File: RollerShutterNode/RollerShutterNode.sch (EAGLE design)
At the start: 32 parts, among them IC2 AT25DF512C-SSHN-B, U1 MMBT2222A-7-F, U2 MMBT2222A-7-F, U3 LM321

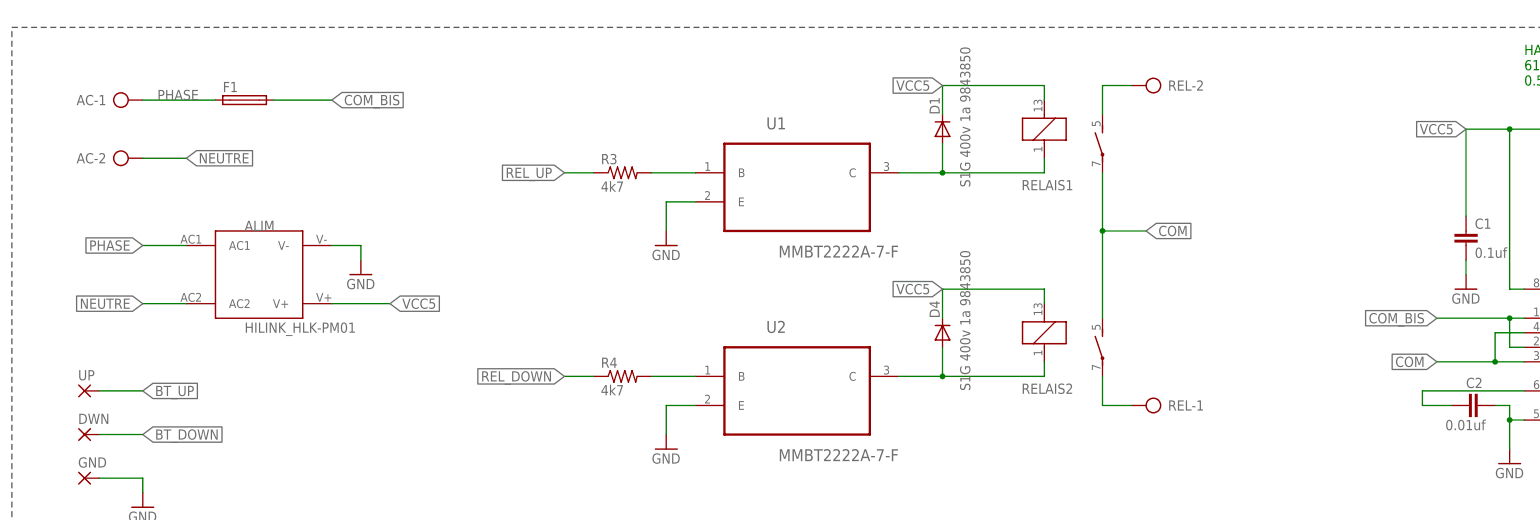
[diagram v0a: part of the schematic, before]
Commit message: fuse removed, added 12-220v motor control
Need to use external fuse and snubber if needed
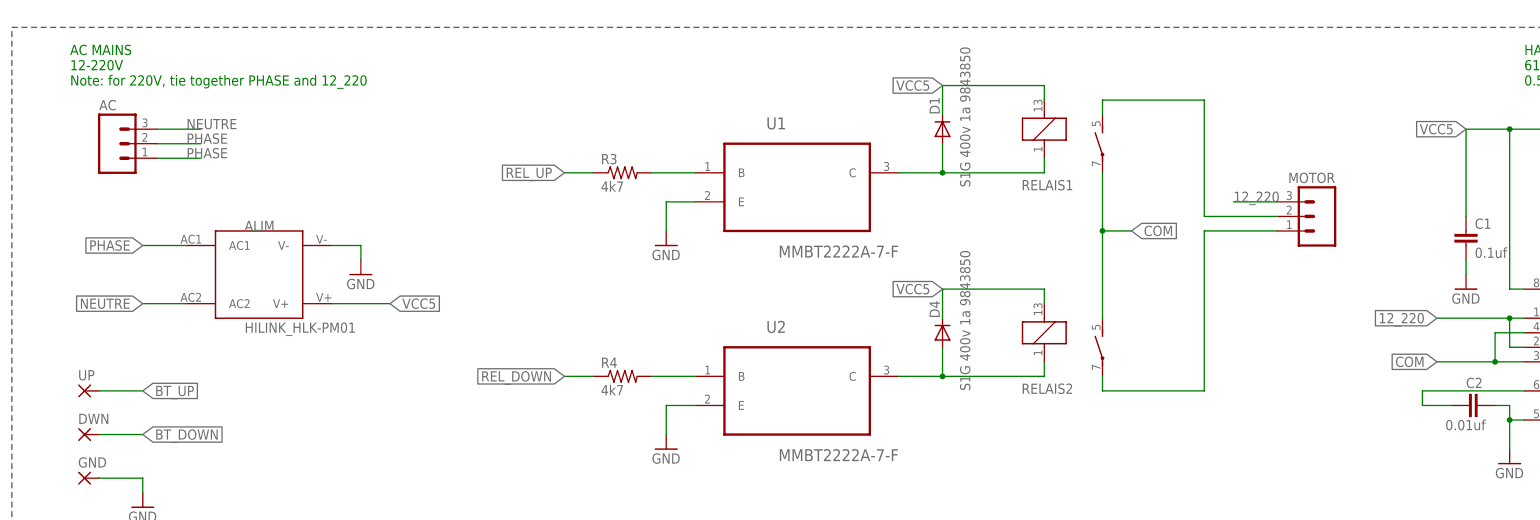
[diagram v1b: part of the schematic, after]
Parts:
- removed F1: (no value), fuse:TE5
- removed REL: (no value), ProgrammateurFilPilote_1.2:AK500/2
- added MOTOR: (no value), SparkFun-Connectors:M03SCREW
- AC: device ProgrammateurFilPilote_1.2:AK500/2 -> SparkFun-Connectors:M03SCREW
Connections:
- removed net COM_BIS: ACS1.IP+, ACS1.IP+_2, F1.2
- new net 12_220: ACS1.IP+, ACS1.IP+_2, MOTOR.3
- net N$7: now also MOTOR.2; no longer REL-2.KL
- net N$9: now also MOTOR.1; no longer REL-1.KL
- net NEUTRE: now also AC.3; no longer AC-2.KL
- net PHASE: now also AC.1, AC.2; no longer AC-1.KL, F1.1
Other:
- note added: "AC MAINS 12-220V Note: for 220V, tie together PHASE and 12_220"
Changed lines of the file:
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@@
 <attribute name="OC_NEWARK" value=""/>
 </part>
-<part name="F1" library="fuse" deviceset="TE5" device=""/>
 <part name="R4" library="SparkFun-Resistors" deviceset="RESISTOR" device="1206" value="4k7"/>
 <part name="GND15" library="supply1" deviceset="GND" device=""/>
@@
 <part name="U1" library="pmo_lib" deviceset="MMBT2222A-7-F" device=""/>
 <part name="U2" library="pmo_lib" deviceset="MMBT2222A-7-F" device=""/>
-<part name="AC" library="ProgrammateurFilPilote_1.2" deviceset="AK500/2" device=""/>
-<part name="REL" library="ProgrammateurFilPilote_1.2" deviceset="AK500/2" device=""/>
 <part name="ALIM" library="pmo_lib" deviceset="HILINK_HLK-PM01" device=""/>
 <part name="GND1" library="SparkFun-Aesthetics" deviceset="GND" device=""/>
@@
 <part name="GND4" library="SparkFun-Aesthetics" deviceset="GND" device=""/>
 <part name="ANT_RFM" library="wirepad" deviceset="SMD2" device=""/>
+<part name="AC" library="SparkFun-Connectors" deviceset="M03" device="SCREW"/>
+<part name="MOTOR" library="SparkFun-Connectors" deviceset="M03" device="SCREW"/>
 </parts>
 <sheets>
@@
 610mV/A
 0.5A -&gt; 93 of 1023 ADC 10bits</text>
+<text x="-33.02" y="106.68" size="1.778" layer="91">AC MAINS
+12-220V
+Note: for 220V, tie together PHASE and 12_220</text>
 </plain>
 <instances>
@@
 </instance>
 <instance part="RELAIS1" gate="2" x="147.32" y="96.52" smashed="yes"/>
-<instance part="F1" gate="1" x="-2.54" y="104.14"/>
 <instance part="R4" gate="G$1" x="63.5" y="55.88"/>
 <instance part="GND15" gate="1" x="71.12" y="43.18"/>
@@
 <instance part="U1" gate="A" x="93.98" y="91.44"/>
 <instance part="U2" gate="A" x="93.98" y="55.88"/>
-<instance part="AC" gate="-1" x="-25.4" y="104.14"/>
-<instance part="AC" gate="-2" x="-25.4" y="93.98"/>
-<instance part="REL" gate="-1" x="157.48" y="50.8" rot="R180"/>
-<instance part="REL" gate="-2" x="157.48" y="106.68" rot="R180"/>
 <instance part="ALIM" gate="G$1" x="0" y="73.66"/>
 <instance part="GND1" gate="1" x="17.78" y="73.66"/>
@@
 <instance part="GND4" gate="1" x="60.96" y="-33.02"/>
 <instance part="ANT_RFM" gate="1" x="233.68" y="-15.24" rot="R270"/>
+<instance part="AC" gate="G$1" x="-25.4" y="96.52"/>
+<instance part="MOTOR" gate="G$1" x="185.42" y="83.82" rot="MR0"/>
 </instances>
 <busses>
@@
 </segment>
 </net>
-<net name="COM_BIS" class="0">
-<segment>
-<pinref part="ACS1" gate="A" pin="IP+_2"/>
-<wire x1="220.98" y1="66.04" x2="218.44" y2="66.04" width="0.1524" layer="91"/>
-<wire x1="218.44" y1="66.04" x2="218.44" y2="60.96" width="0.1524" layer="91"/>
-<pinref part="ACS1" gate="A" pin="IP+"/>
-<wire x1="218.44" y1="60.96" x2="220.98" y2="60.96" width="0.1524" layer="91"/>
-<junction x="218.44" y="66.04"/>
-<wire x1="218.44" y1="66.04" x2="205.74" y2="66.04" width="0.1524" layer="91"/>
-<label x="205.74" y="66.04" size="1.778" layer="95" rot="R180" xref="yes"/>
-</segment>
-<segment>
-<wire x1="2.54" y1="104.14" x2="12.7" y2="104.14" width="0.1524" layer="91"/>
-<label x="12.7" y="104.14" size="1.778" layer="95" xref="yes"/>
-<pinref part="F1" gate="1" pin="2"/>
-</segment>
-</net>
 <net name="N$4" class="0">
 <segment>
@@
 <junction x="147.32" y="81.28"/>
 <wire x1="147.32" y1="81.28" x2="147.32" y2="66.04" width="0.1524" layer="91"/>
-<wire x1="147.32" y1="81.28" x2="154.94" y2="81.28" width="0.1524" layer="91"/>
-<label x="154.94" y="81.28" size="1.778" layer="95" xref="yes"/>
+<wire x1="147.32" y1="81.28" x2="152.4" y2="81.28" width="0.1524" layer="91"/>
+<label x="152.4" y="81.28" size="1.778" layer="95" xref="yes"/>
 </segment>
 <segment>
@@
 <net name="PHASE" class="0">
 <segment>
-<pinref part="AC" gate="-1" pin="KL"/>
-<pinref part="F1" gate="1" pin="1"/>
-<wire x1="-20.32" y1="104.14" x2="-7.62" y2="104.14" width="0.1524" layer="91"/>
-<label x="-17.78" y="104.14" size="1.778" layer="95"/>
-</segment>
-<segment>
 <pinref part="ALIM" gate="G$1" pin="AC1"/>
 <wire x1="-12.7" y1="78.74" x2="-20.32" y2="78.74" width="0.1524" layer="91"/>
 <label x="-20.32" y="78.74" size="1.778" layer="95" rot="R180" xref="yes"/>
 </segment>
+<segment>
+<pinref part="AC" gate="G$1" pin="2"/>
+<wire x1="-17.78" y1="96.52" x2="-10.16" y2="96.52" width="0.1524" layer="91"/>
+<label x="-12.7" y="96.52" size="1.778" layer="95"/>
+</segment>
+<segment>
+<pinref part="AC" gate="G$1" pin="1"/>
+<wire x1="-17.78" y1="93.98" x2="-10.16" y2="93.98" width="0.1524" layer="91"/>
+<label x="-12.7" y="93.98" size="1.778" layer="95"/>
+</segment>
 </net>
 <net name="NEUTRE" class="0">
-<segment>
-<pinref part="AC" gate="-2" pin="KL"/>
-<wire x1="-20.32" y1="93.98" x2="-12.7" y2="93.98" width="0.1524" layer="91"/>
-<label x="-12.7" y="93.98" size="1.778" layer="95" xref="yes"/>
-</segment>
 <segment>
 <pinref part="ALIM" gate="G$1" pin="AC2"/>
@@
 <label x="-20.32" y="68.58" size="1.778" layer="95" rot="R180" xref="yes"/>
 </segment>
-</net>
-<net name="N$7" class="0">
-<segment>
-<pinref part="RELAIS1" gate="2" pin="S"/>
-<wire x1="147.32" y1="101.6" x2="147.32" y2="106.68" width="0.1524" layer="91"/>
-<pinref part="REL" gate="-2" pin="KL"/>
-<wire x1="152.4" y1="106.68" x2="147.32" y2="106.68" width="0.1524" layer="91"/>
-</segment>
-</net>
-<net name="N$9" class="0">
-<segment>
-<pinref part="RELAIS2" gate="2" pin="P"/>
-<wire x1="147.32" y1="55.88" x2="147.32" y2="50.8" width="0.1524" layer="91"/>
-<pinref part="REL" gate="-1" pin="KL"/>
-<wire x1="152.4" y1="50.8" x2="147.32" y2="50.8" width="0.1524" layer="91"/>
+<segment>
+<pinref part="AC" gate="G$1" pin="3"/>
+<wire x1="-17.78" y1="99.06" x2="-10.16" y2="99.06" width="0.1524" layer="91"/>
+<label x="-12.7" y="99.06" size="1.778" layer="95"/>
 </segment>
 </net>
@@
 </segment>
 </net>
+<net name="12_220" class="0">
+<segment>
+<pinref part="ACS1" gate="A" pin="IP+_2"/>
+<wire x1="220.98" y1="66.04" x2="218.44" y2="66.04" width="0.1524" layer="91"/>
+<wire x1="218.44" y1="66.04" x2="218.44" y2="60.96" width="0.1524" layer="91"/>
+<pinref part="ACS1" gate="A" pin="IP+"/>
+<wire x1="218.44" y1="60.96" x2="220.98" y2="60.96" width="0.1524" layer="91"/>
+<junction x="218.44" y="66.04"/>
+<wire x1="218.44" y1="66.04" x2="205.74" y2="66.04" width="0.1524" layer="91"/>
+<label x="205.74" y="66.04" size="1.778" layer="95" rot="R180" xref="yes"/>
+</segment>
+<segment>
+<pinref part="MOTOR" gate="G$1" pin="3"/>
+<wire x1="177.8" y1="86.36" x2="170.18" y2="86.36" width="0.1524" layer="91"/>
+<label x="170.18" y="86.36" size="1.778" layer="95"/>
+</segment>
+</net>
+<net name="N$7" class="0">
+<segment>
+<wire x1="165.1" y1="83.82" x2="165.1" y2="104.14" width="0.1524" layer="91"/>
+<pinref part="RELAIS1" gate="2" pin="S"/>
+<wire x1="165.1" y1="104.14" x2="147.32" y2="104.14" width="0.1524" layer="91"/>
+<wire x1="147.32" y1="104.14" x2="147.32" y2="101.6" width="0.1524" layer="91"/>
+<pinref part="MOTOR" gate="G$1" pin="2"/>
+<wire x1="177.8" y1="83.82" x2="165.1" y2="83.82" width="0.1524" layer="91"/>
+</segment>
+</net>
+<net name="N$9" class="0">
+<segment>
+<pinref part="RELAIS2" gate="2" pin="P"/>
+<wire x1="165.1" y1="53.34" x2="147.32" y2="53.34" width="0.1524" layer="91"/>
+<wire x1="147.32" y1="53.34" x2="147.32" y2="55.88" width="0.1524" layer="91"/>
+<pinref part="MOTOR" gate="G$1" pin="1"/>
+<wire x1="177.8" y1="81.28" x2="165.1" y2="81.28" width="0.1524" layer="91"/>
+<wire x1="165.1" y1="81.28" x2="165.1" y2="53.34" width="0.1524" layer="91"/>
+</segment>
+</net>

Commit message: change
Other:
- note removed: "AC MAINS 12-220V Note: for 220V, tie together PHASE and 12_220"
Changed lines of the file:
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@@
 <grid distance="0.1" unitdist="inch" unit="inch" style="lines" multiple="1" display="no" altdistance="0.01" altunitdist="inch" altunit="inch"/>
 <layers>
-<layer number="1" name="Top" color="4" fill="1" visible="yes" active="no"/>
-<layer number="2" name="Route2" color="1" fill="3" visible="yes" active="no"/>
-<layer number="3" name="Route3" color="4" fill="3" visible="yes" active="no"/>
-<layer number="4" name="Route4" color="1" fill="4" visible="yes" active="no"/>
-<layer number="5" name="Route5" color="4" fill="4" visible="yes" active="no"/>
-<layer number="6" name="Route6" color="1" fill="8" visible="yes" active="no"/>
-<layer number="7" name="Route7" color="4" fill="8" visible="yes" active="no"/>
-<layer number="8" name="Route8" color="1" fill="2" visible="yes" active="no"/>
-<layer number="9" name="Route9" color="4" fill="2" visible="yes" active="no"/>
-<layer number="10" name="Route10" color="1" fill="7" visible="yes" active="no"/>
-<layer number="11" name="Route11" color="4" fill="7" visible="yes" active="no"/>
-<layer number="12" name="Route12" color="1" fill="5" visible="yes" active="no"/>
-<layer number="13" name="Route13" color="4" fill="5" visible="yes" active="no"/>
-<layer number="14" name="Route14" color="1" fill="6" visible="yes" active="no"/>
-<layer number="15" name="Route15" color="4" fill="6" visible="yes" active="no"/>
-<layer number="16" name="Bottom" color="1" fill="1" visible="yes" active="no"/>
-<layer number="17" name="Pads" color="2" fill="1" visible="yes" active="no"/>
-<layer number="18" name="Vias" color="2" fill="1" visible="yes" active="no"/>
-<layer number="19" name="Unrouted" color="6" fill="1" visible="yes" active="no"/>
-<layer number="20" name="Dimension" color="15" fill="1" visible="yes" active="no"/>
-<layer number="21" name="tPlace" color="7" fill="1" visible="yes" active="no"/>
-<layer number="22" name="bPlace" color="7" fill="1" visible="yes" active="no"/>
-<layer number="23" name="tOrigins" color="15" fill="1" visible="yes" active="no"/>
-<layer number="24" name="bOrigins" color="15" fill="1" visible="yes" active="no"/>
-<layer number="25" name="tNames" color="7" fill="1" visible="yes" active="no"/>
-<layer number="26" name="bNames" color="7" fill="1" visible="yes" active="no"/>
-<layer number="27" name="tValues" color="7" fill="1" visible="yes" active="no"/>
-<layer number="28" name="bValues" color="7" fill="1" visible="yes" active="no"/>
+<layer number="1" name="Top" color="4" fill="1" visible="no" active="no"/>
+<layer number="2" name="Route2" color="1" fill="3" visible="no" active="no"/>
+<layer number="3" name="Route3" color="4" fill="3" visible="no" active="no"/>
+<layer number="4" name="Route4" color="1" fill="4" visible="no" active="no"/>
+<layer number="5" name="Route5" color="4" fill="4" visible="no" active="no"/>
+<layer number="6" name="Route6" color="1" fill="8" visible="no" active="no"/>
+<layer number="7" name="Route7" color="4" fill="8" visible="no" active="no"/>
+<layer number="8" name="Route8" color="1" fill="2" visible="no" active="no"/>
+<layer number="9" name="Route9" color="4" fill="2" visible="no" active="no"/>
+<layer number="10" name="Route10" color="1" fill="7" visible="no" active="no"/>
+<layer number="11" name="Route11" color="4" fill="7" visible="no" active="no"/>
+<layer number="12" name="Route12" color="1" fill="5" visible="no" active="no"/>
+<layer number="13" name="Route13" color="4" fill="5" visible="no" active="no"/>
+<layer number="14" name="Route14" color="1" fill="6" visible="no" active="no"/>
+<layer number="15" name="Route15" color="4" fill="6" visible="no" active="no"/>
+<layer number="16" name="Bottom" color="1" fill="1" visible="no" active="no"/>
+<layer number="17" name="Pads" color="2" fill="1" visible="no" active="no"/>
+<layer number="18" name="Vias" color="2" fill="1" visible="no" active="no"/>
+<layer number="19" name="Unrouted" color="6" fill="1" visible="no" active="no"/>
+<layer number="20" name="Dimension" color="15" fill="1" visible="no" active="no"/>
+<layer number="21" name="tPlace" color="7" fill="1" visible="no" active="no"/>
+<layer number="22" name="bPlace" color="7" fill="1" visible="no" active="no"/>
+<layer number="23" name="tOrigins" color="15" fill="1" visible="no" active="no"/>
+<layer number="24" name="bOrigins" color="15" fill="1" visible="no" active="no"/>
+<layer number="25" name="tNames" color="7" fill="1" visible="no" active="no"/>
+<layer number="26" name="bNames" color="7" fill="1" visible="no" active="no"/>
+<layer number="27" name="tValues" color="7" fill="1" visible="no" active="no"/>
+<layer number="28" name="bValues" color="7" fill="1" visible="no" active="no"/>
 <layer number="29" name="tStop" color="7" fill="3" visible="no" active="no"/>
 <layer number="30" name="bStop" color="7" fill="6" visible="no" active="no"/>
@@
 <layer number="35" name="tGlue" color="7" fill="4" visible="no" active="no"/>
 <layer number="36" name="bGlue" color="7" fill="5" visible="no" active="no"/>
-<layer number="37" name="tTest" color="7" fill="1" visible="yes" active="no"/>
-<layer number="38" name="bTest" color="7" fill="1" visible="yes" active="no"/>
+<layer number="37" name="tTest" color="7" fill="1" visible="no" active="no"/>
+<layer number="38" name="bTest" color="7" fill="1" visible="no" active="no"/>
 <layer number="39" name="tKeepout" color="4" fill="11" visible="no" active="no"/>
 <layer number="40" name="bKeepout" color="1" fill="11" visible="no" active="no"/>
@@
 <layer number="44" name="Drills" color="7" fill="1" visible="no" active="no"/>
 <layer number="45" name="Holes" color="7" fill="1" visible="no" active="no"/>
-<layer number="46" name="Milling" color="3" fill="1" visible="yes" active="no"/>
-<layer number="47" name="Measures" color="7" fill="1" visible="yes" active="no"/>
-<layer number="48" name="Document" color="7" fill="1" visible="yes" active="no"/>
-<layer number="49" name="Reference" color="7" fill="1" visible="yes" active="no"/>
-<layer number="50" name="dxf" color="7" fill="1" visible="yes" active="no"/>
-<layer number="51" name="tDocu" color="7" fill="1" visible="yes" active="no"/>
-<layer number="52" name="bDocu" color="7" fill="1" visible="yes" active="no"/>
-<layer number="53" name="tGND_GNDA" color="7" fill="9" visible="yes" active="no"/>
-<layer number="54" name="bGND_GNDA" color="1" fill="9" visible="yes" active="no"/>
-<layer number="56" name="wert" color="7" fill="1" visible="yes" active="no"/>
-<layer number="57" name="tCAD" color="7" fill="1" visible="yes" active="no"/>
+<layer number="46" name="Milling" color="3" fill="1" visible="no" active="no"/>
+<layer number="47" name="Measures" color="7" fill="1" visible="no" active="no"/>
+<layer number="48" name="Document" color="7" fill="1" visible="no" active="no"/>
+<layer number="49" name="Reference" color="7" fill="1" visible="no" active="no"/>
+<layer number="50" name="dxf" color="7" fill="1" visible="no" active="no"/>
+<layer number="51" name="tDocu" color="7" fill="1" visible="no" active="no"/>
+<layer number="52" name="bDocu" color="7" fill="1" visible="no" active="no"/>
+<layer number="53" name="tGND_GNDA" color="7" fill="9" visible="no" active="no"/>
+<layer number="54" name="bGND_GNDA" color="1" fill="9" visible="no" active="no"/>
+<layer number="56" name="wert" color="7" fill="1" visible="no" active="no"/>
+<layer number="57" name="tCAD" color="7" fill="1" visible="no" active="no"/>
 <layer number="90" name="Modules" color="5" fill="1" visible="yes" active="yes"/>
 <layer number="91" name="Nets" color="2" fill="1" visible="yes" active="yes"/>
@@
 610mV/A
 0.5A -&gt; 93 of 1023 ADC 10bits</text>
-<text x="-33.02" y="106.68" size="1.778" layer="91">AC MAINS
-12-220V
-Note: for 220V, tie together PHASE and 12_220</text>
 </plain>
 <instances>
